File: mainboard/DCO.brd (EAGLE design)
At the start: 75 x 22 mm, 44 parts, among them IC101 LF353D, IC201 LF353D, P101 TRIMPOT 100K

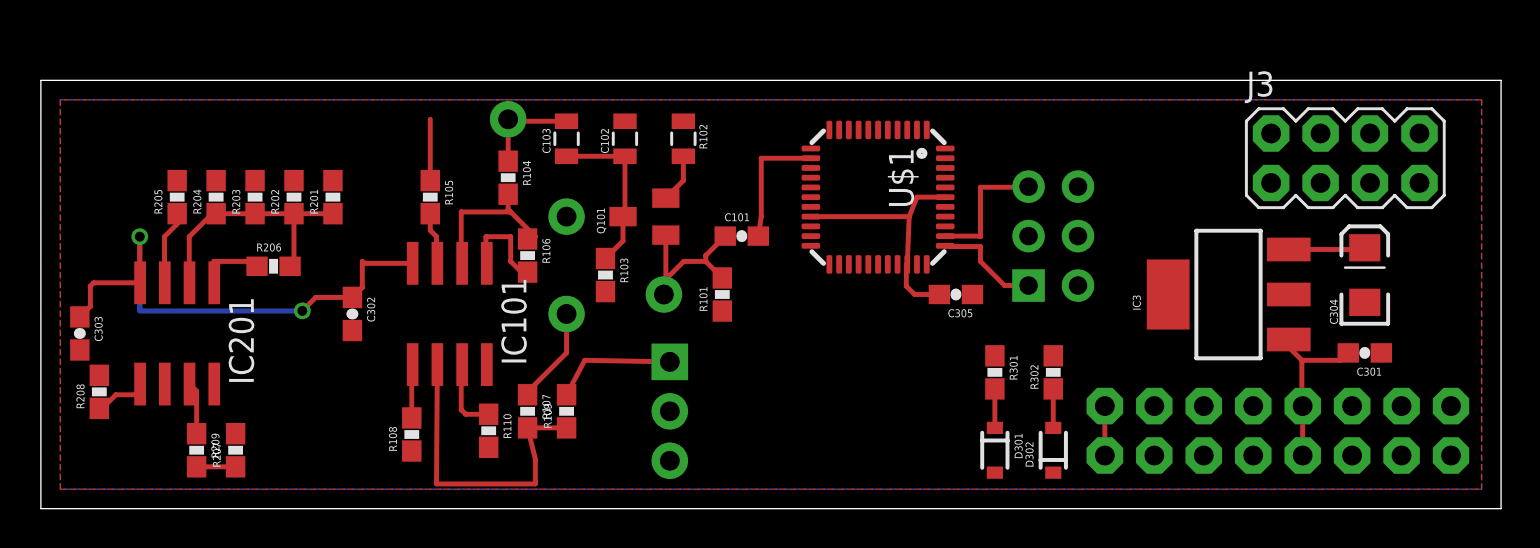
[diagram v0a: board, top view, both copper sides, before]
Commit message: Re-laid out board, no routing
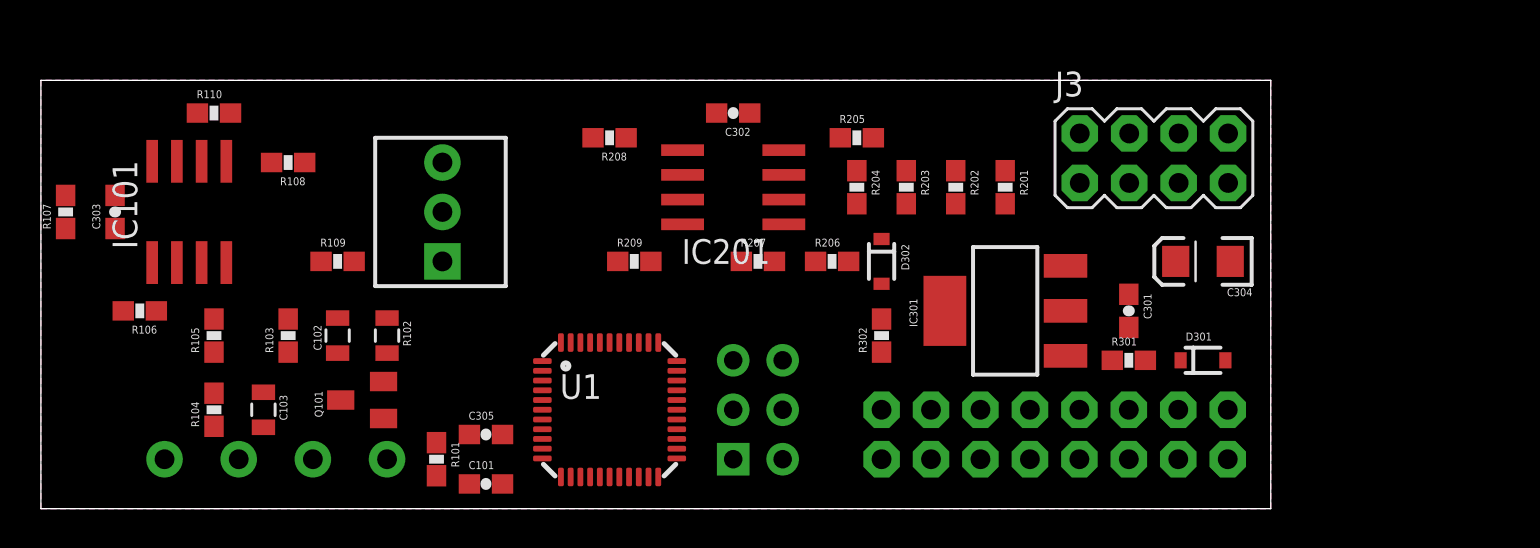
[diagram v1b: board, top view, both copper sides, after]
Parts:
- removed IC3: (no value), SparkFun:SOT223
- removed U$1: XMEGA-A4VQFN, custom:QFN44
- added IC301: (no value), SparkFun:SOT223
- added U1: XMEGA-A4VQFN, custom:QFN44
- moved R205 35.0 mm to (41.9, 19.1), turned to 0 degrees
- moved R201 34.5 mm to (49.5, 16.5), turned to 270 degrees
- moved R202 34.0 mm to (47.0, 16.5), turned to 270 degrees
- moved R203 33.5 mm to (44.5, 16.5), turned to 270 degrees
- moved R204 32.9 mm to (41.9, 16.5), turned to 270 degrees
- moved IC201 29.5 mm to (35.6, 16.5), turned to 90 degrees
- moved R208 29.3 mm to (29.2, 19.1), turned to 180 degrees
- moved R206 28.7 mm to (40.6, 12.7)
- moved R207 28.5 mm to (36.8, 12.7), turned to 0 degrees
- moved R107 25.8 mm to (1.27, 15.2), turned to 90 degrees
- moved C305 25.2 mm to (22.9, 3.81), turned to 0 degrees
- moved R209 24.5 mm to (30.5, 12.7), turned to 0 degrees
- moved TP103 22.3 mm to (10.2, 2.54)
- moved C302 22.1 mm to (35.6, 20.3), turned to 180 degrees
- moved TP104 22.0 mm to (6.35, 2.54)
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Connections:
- net +12V: now also IC301.1; no longer IC3.1
- net +3V3: now also IC301.3, U1.19, U1.31, U1.39, U1.9; no longer IC3.3, U$1.19, U$1.31, U$1.39, U$1.9
- net ADC_IN: now also U1.40; no longer U$1.40
- net FREQ: now also U1.13; no longer U$1.13
- net FREQCV: now also U1.7; no longer U$1.7
- net GND: now also IC301.2, U1.18, U1.30, U1.38, U1.8; no longer IC3.2, U$1.18, U$1.30, U$1.38, U$1.8
- net PDI_DATA: now also U1.34; no longer U$1.34
- net RESET: now also U1.35; no longer U$1.35
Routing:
- net -12V: track 29.0 -> 0.00 mm, vias 2 -> 0
- net +3V3: track 17.0 -> 0.00 mm
- net N$3: track 16.1 -> 0.00 mm
- net R205: track 13.0 -> 0.00 mm
- net N$13: track 10.0 -> 0.00 mm
- net +12V: track 9.17 -> 0.00 mm
- net N$1: track 8.66 -> 0.00 mm
- net N$2: track 8.44 -> 0.00 mm
- net R104: track 8.41 -> 0.00 mm
- net RESET: track 6.84 -> 0.00 mm
- net FREQ: track 6.56 -> 0.00 mm
- net N$12: track 6.37 -> 0.00 mm
- net PDI_DATA: track 5.57 -> 0.00 mm
- net N$5: track 5.19 -> 0.00 mm
- net N$11: track 3.99 -> 0.00 mm
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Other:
- board size 75 x 22 mm -> 63.2 x 22 mm

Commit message: edited schematic parts after sourcing from mouser, initial board layout.
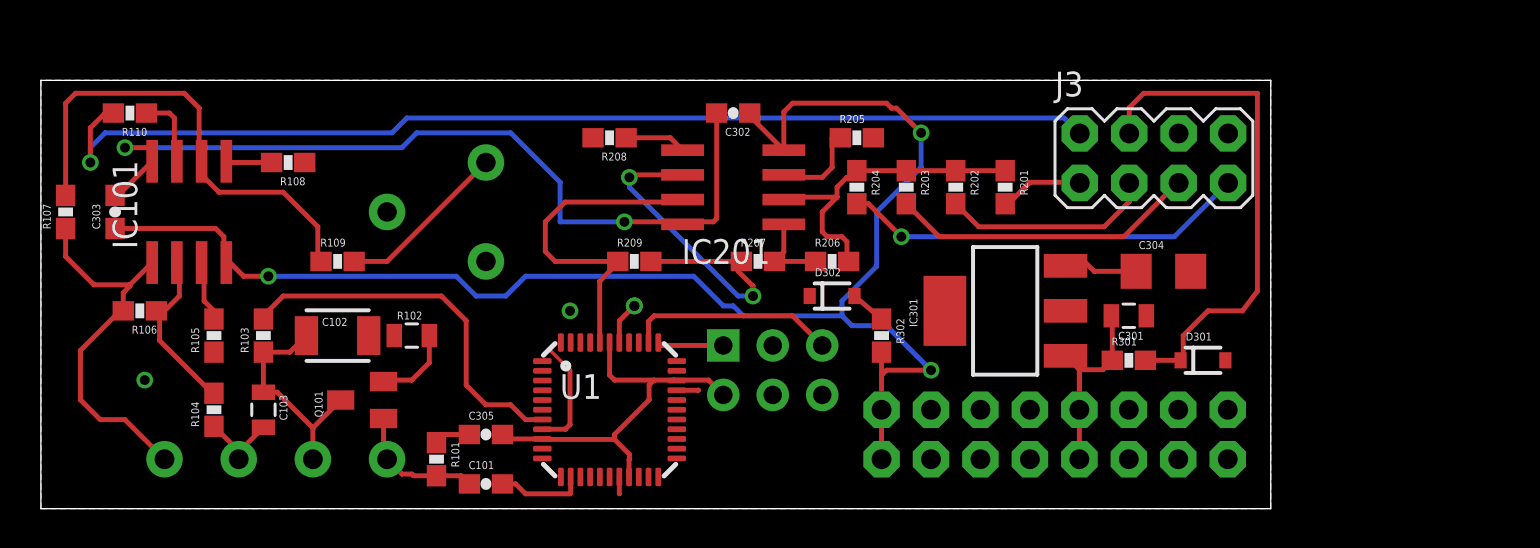
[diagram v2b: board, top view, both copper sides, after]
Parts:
- C102: device SparkFun:0805 -> SparkFun:1210
- C301: device SparkFun:0603-CAP -> SparkFun:0805
- C304: device SparkFun:EIA3216 -> SparkFun:1206
- P101: device SparkFun:3362U-2 -> SparkFun:TRIM_POT_PTH
- R207: value 50K -> 51K
- moved R110 4.32 mm to (4.57, 20.3), turned to 180 degrees
- moved D302 3.10 mm to (40.6, 10.9), turned to 0 degrees
- moved H1 2.17 mm to (37.6, 7.11), turned to 270 degrees
- moved C304 2.09 mm to (57.7, 12.2), turned to 0 degrees
- moved R102 1.27 mm to (19.1, 8.89), turned to 0 degrees
- moved R103 1.27 mm to (11.4, 8.89)
- moved C301 0.25 mm to (55.9, 9.91), turned to 180 degrees
- turned C102 to 0 degrees
- flipped P101 to the bottom, turned to 270 degrees
- turned R302 to 270 degrees
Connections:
- net +3V3: now also C304.1; no longer C304.A
- net GND: now also C304.2; no longer C304.C
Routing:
- net -12V: track 0.00 -> 78.4 mm, vias 0 -> 3
- net +12V: track 0.00 -> 57.4 mm, vias 0 -> 2
- net OUT: track 0.00 -> 55.8 mm, vias 0 -> 1
- net +5V: track 0.00 -> 26.4 mm
- net N$3: track 0.00 -> 24.5 mm
- net +3V3: track 0.00 -> 24.0 mm
- net FINE: track 0.00 -> 20.9 mm, vias 0 -> 1
- net N$13: track 0.00 -> 19.6 mm
- net FREQCV: track 0.00 -> 19.5 mm
- net N$19: track 0.00 -> 18.8 mm, vias 0 -> 2
- net ADC_IN: track 0.00 -> 17.5 mm
- net R205: track 0.00 -> 17.1 mm
- net COARSE: track 0.00 -> 15.8 mm
- net GND: track 0.00 -> 11.8 mm, vias 0 -> 4
- net N$1: track 0.00 -> 11.6 mm
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
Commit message: brendan said it was a good idea to add a ground via near the decoupling cap for the micro
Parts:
- moved C304 1.52 mm to (59.2, 12.2)
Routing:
- net +12V: track 57.4 -> 112.6 mm, vias 2 -> 4
- net +3V3: track 24.0 -> 55.9 mm, vias 0 -> 1
- net -5V: track 1.82 -> 30.8 mm, vias 0 -> 1
- net N$11: track 3.82 -> 17.6 mm, vias 0 -> 1
- net FINE: track 20.9 -> 22.4 mm
- net -12V: track 78.4 -> 77.6 mm
- net GND: track 11.8 -> 12.0 mm, vias 4 -> 7

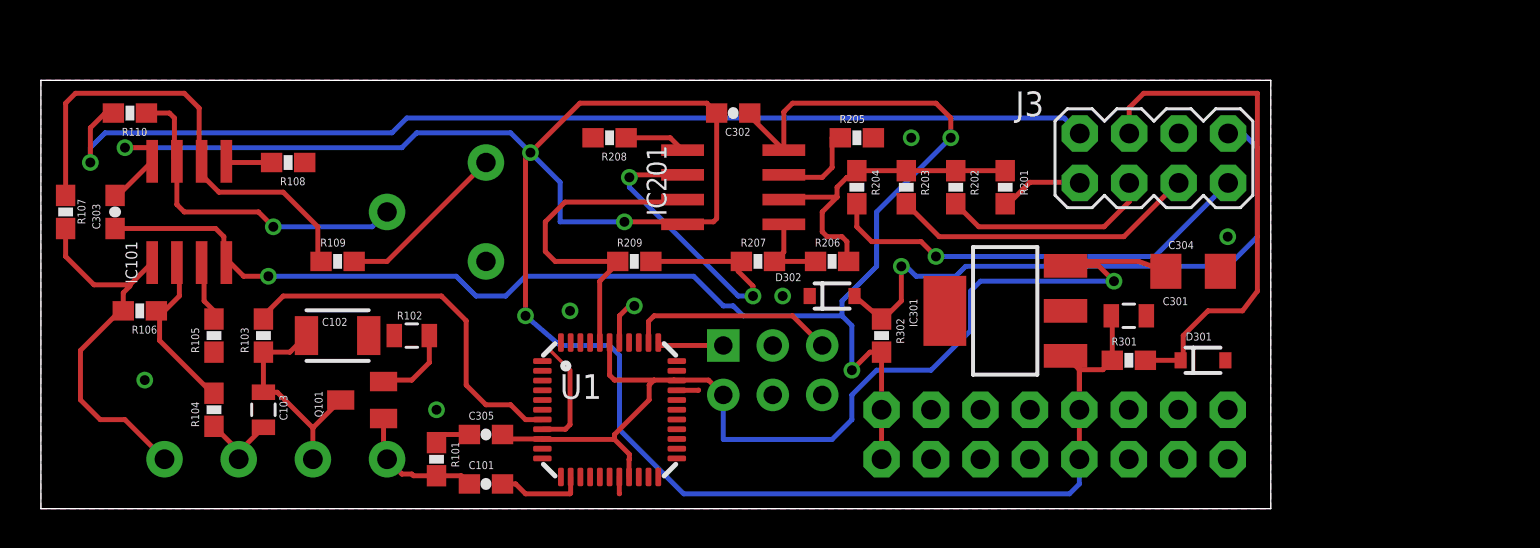
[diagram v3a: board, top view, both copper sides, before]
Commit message: Another attempt to layout DCO.
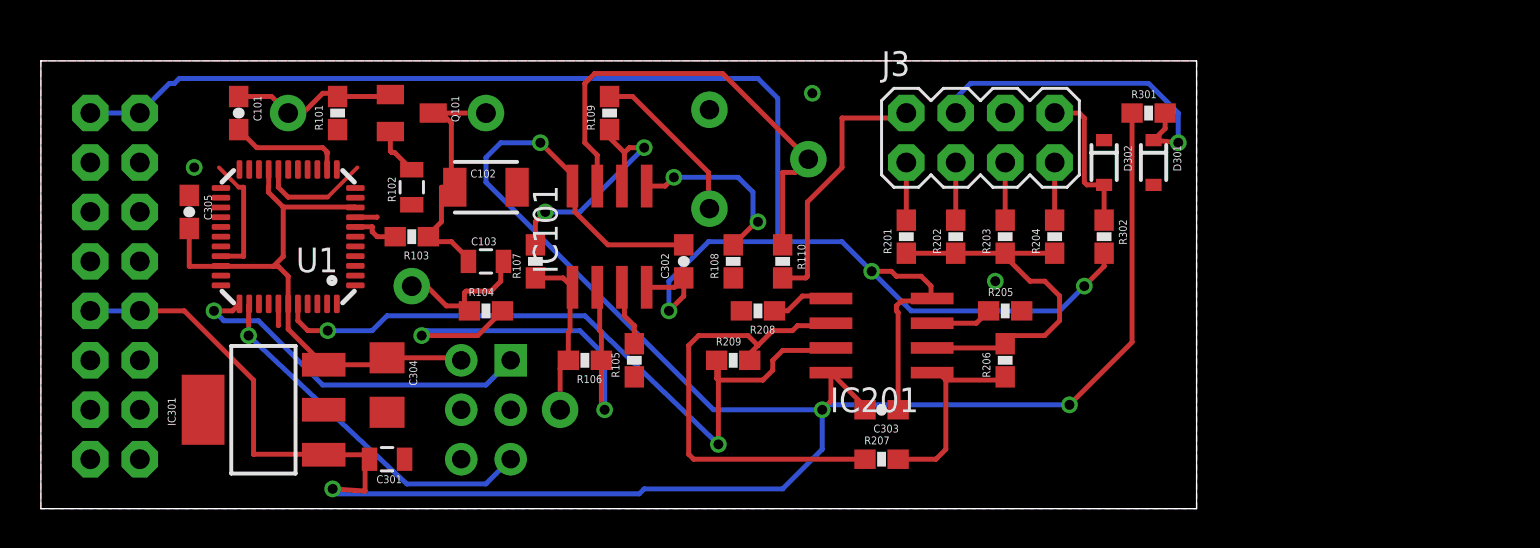
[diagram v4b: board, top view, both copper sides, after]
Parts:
- moved POWER 46.8 mm to (3.81, 14.0), turned to 270 degrees
- moved C304 41.8 mm to (17.8, 6.35), turned to 270 degrees
- moved C303 40.7 mm to (43.2, 5.08), turned to 180 degrees
- moved C301 38.8 mm to (17.8, 2.54)
- moved IC301 38.4 mm to (11.4, 5.08)
- moved R110 34.4 mm to (38.1, 12.7), turned to 270 degrees
- moved R107 24.3 mm to (25.4, 12.7)
- moved R108 23.4 mm to (35.6, 12.7), turned to 90 degrees
- moved R106 23.0 mm to (27.9, 7.62)
- moved C101 22.9 mm to (10.2, 20.3), turned to 270 degrees
- moved IC101 21.6 mm to (29.2, 14.0)
- moved R105 21.6 mm to (30.5, 7.62)
- moved TP104 20.5 mm to (26.7, 5.08)
- moved TP102 19.9 mm to (22.9, 20.3)
- moved C305 19.0 mm to (7.62, 15.2), turned to 270 degrees
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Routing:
- net OUT: track 55.8 -> 13.6 mm, vias 1 -> 0
- net +3V3: track 55.9 -> 29.0 mm, vias 1 -> 0
- net -5V: track 30.8 -> 7.81 mm, vias 1 -> 0
- net ADC_IN: track 17.5 -> 37.8 mm, vias 0 -> 2
- net FINE: track 22.4 -> 2.96 mm, vias 1 -> 0
- net FREQCV: track 19.5 -> 2.41 mm
- net PDI_DATA: track 3.40 -> 18.8 mm, vias 0 -> 1
- net R104: track 8.78 -> 23.9 mm, vias 0 -> 2
- net COARSE: track 15.8 -> 2.96 mm
- net N$3: track 24.5 -> 12.7 mm, vias 0 -> 2
- net N$13: track 19.6 -> 8.66 mm
- net +12V: track 112.6 -> 122.6 mm
- net -12V: track 77.6 -> 87.5 mm
- net +5V: track 26.4 -> 17.6 mm, vias 0 -> 1
- net AUX_IN: track 10.9 -> 2.96 mm
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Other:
- board size 63.2 x 22 mm -> 59.4 x 23 mm
